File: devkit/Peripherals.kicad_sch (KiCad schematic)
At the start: 50 parts, among them IC501 APDS-9306-065, IC502 BMI270, IC503 LIS2MDLTR, IC504 BMP581, IC505 DRV2603RUNT, IC506 PCA9306JK, IC507 RV-8263-C8, J501 Jumper, J502 Jumper, J503 Jumper, J504 Jumper, J505 Jumper, J506 Jumper, J507 Jumper, M501 Vibrator DC Motor, X501 Current, X502 I2S, X503 Current, X504 I2C, X505 Current, X506 Current, X507 Current, X508 Current, X509 Motor, X510 Current

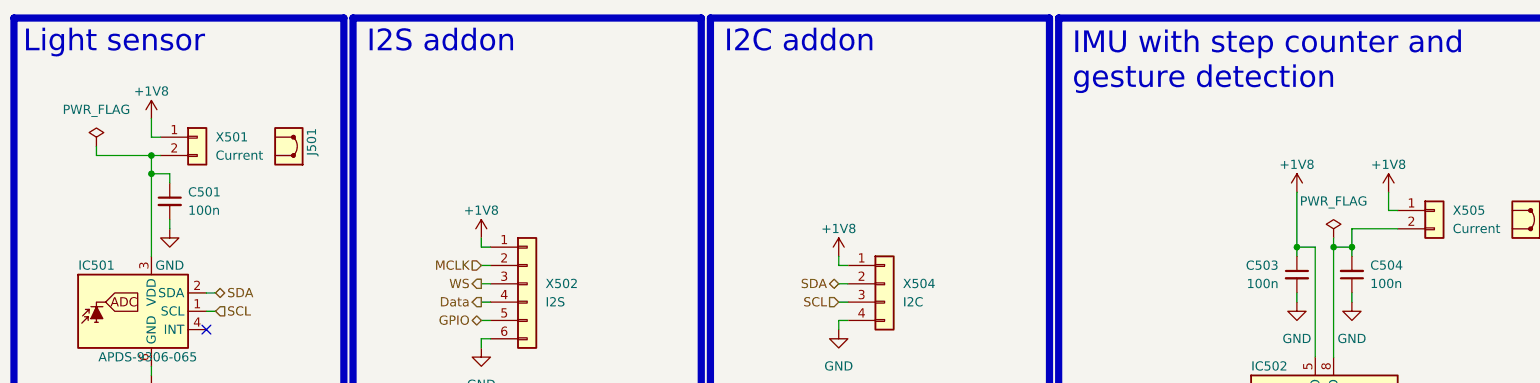
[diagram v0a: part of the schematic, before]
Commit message: Bug: Issue #198
- Change 3V0 to 3V3 to prevent flickering display

Closes: #198

Signed-off-by: Daniel Kampert <DanielKampert@kampis-elektroecke.de>
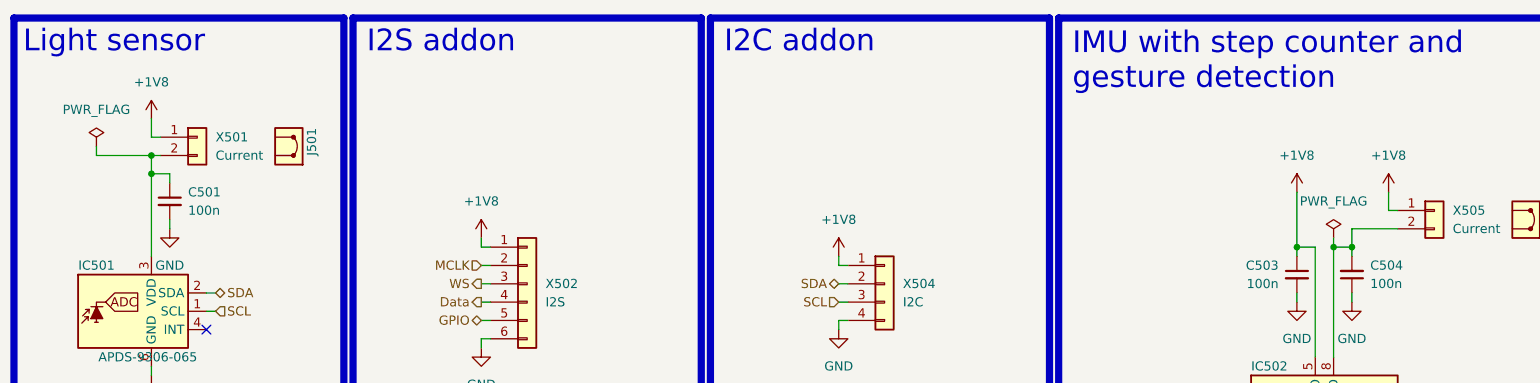
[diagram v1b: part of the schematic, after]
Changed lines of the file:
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@@
 		)
 		(property "Value" "+1V8"
-			(at 191.77 34.29 0)
+			(at 191.77 33.02 0)
 			(effects
 				(font
@@
 		)
 		(property "Value" "+1V8"
-			(at 33.02 24.13 0)
+			(at 33.02 22.86 0)
 			(effects
 				(font
@@
 		)
 		(property "Value" "+1V8"
-			(at 128.27 43.18 0)
+			(at 128.27 41.91 0)
 			(effects
 				(font
@@
 		)
 		(property "Value" "+1V8"
-			(at 204.47 34.29 0)
+			(at 204.47 33.02 0)
 			(effects
 				(font
@@
 		)
 		(property "Value" "+1V8"
-			(at 78.74 40.64 0)
+			(at 78.74 39.37 0)
 			(effects
 				(font
